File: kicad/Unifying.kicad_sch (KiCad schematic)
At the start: 38 parts

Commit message: Add files via upload
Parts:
- C1: renamed from U; value (none) -> 100n 50v; footprint (none) -> Capacitor_SMD:C_0402_1005Metric
- C10, C11, C2: renamed from U; value (none) -> 100n; footprint (none) -> Capacitor_SMD:C_0402_1005Metric
- C12: renamed from U; value (none) -> 1.2nF; footprint (none) -> Capacitor_SMD:C_0402_1005Metric
- C13, C14, C15, C16: renamed from U; value (none) -> 10u; footprint (none) -> Capacitor_SMD:C_0805_2012Metric
- C17: renamed from U; value (none) -> 100uF; footprint (none) -> Capacitor_Tantalum_SMD:CP_EIA-7343-31_Kemet-D
- C4, C5, C6, C7, C8, C9: renamed from U; value (none) -> 10u 10v; footprint (none) -> Capacitor_SMD:C_0805_2012Metric
- D1: renamed from U; value (none) -> MMBZ5242BLT3G; footprint (none) -> Diode_SMD:D_SOT-23_ANK
- H1, H2, H3, H4: renamed from U; value (none) -> MountingHole; footprint (none) -> MountingHole:MountingHole_2.7mm_M2.5
- H5, H6: renamed from U; value (none) -> M.2 Hole; footprint (none) -> MountingHole:M.2Hole_3.5mm
- J1: renamed from U; value (none) -> Conn_01x02; footprint (none) -> TerminalBlock:TerminalBlock_bornier-2_P5.08mm
- J2: renamed from U; value (none) -> Bus_M.2_Socket_B; footprint (none) -> CM4IO:Conn_TE-M.2-0.5-67P-doublesided
- L2: renamed from U; value (none) -> SRN6045TA-3R3Y (3.3uH); footprint (none) -> Inductor_SMD:L_Bourns_SRP7028A_7.3x6.6mm
- Q1: renamed from U; value (none) -> DMP3013SFV-7; footprint (none) -> Package_SON:Diodes_PowerDI3333-8
- R1, R4: renamed from U; value (none) -> 12K 1%; footprint (none) -> Resistor_SMD:R_0402_1005Metric
- R10: renamed from U; value (none) -> 15K 1%; footprint (none) -> Resistor_SMD:R_0402_1005Metric
- R11: renamed from U; value (none) -> 12K; footprint (none) -> Resistor_SMD:R_0402_1005Metric
- R3: renamed from U; value (none) -> 10R; footprint (none) -> Resistor_SMD:R_0402_1005Metric
- R5, R6, R7, R8: renamed from U; value (none) -> nf; footprint (none) -> Resistor_SMD:R_0402_1005Metric
- R9: renamed from U; value (none) -> 47K 1%; footprint (none) -> Resistor_SMD:R_0402_1005Metric
- U2: renamed from U; value (none) -> AP64501SP-13; footprint (none) -> Package_SO:SOIC-8-1EP_3.9x4.9mm_P1.27mm_EP2.95x4.9mm_Mask2.71x3.4mm_ThermalVias
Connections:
- net +3.3v: no longer J2.2 (3.3V), J2.4 (3.3V), J2.70 (3.3V), J2.72 (3.3V), J2.74 (3.3V), R11.2
- net +3.3vSSD: now also J2.2 (3.3V), J2.4 (3.3V), J2.70 (3.3V), J2.72 (3.3V), J2.74 (3.3V), R11.2; no longer R8.1
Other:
- note added: "+5V powers the CM4 module, high-speed connectors and USB connectors CM4 module has it's own 3.3V regulator"
- note added: "Connectors ------- Dual USB A USB OTG internal USB"
- note added: "PSU 5V -> 3.3v @ 3A for M.2"
- note removed: "Connectors ------- Dual USB A USB C OTG internal USB"
- note removed: "PSU 5V -> 3.3v @ 3A mainly for M.2"
- moved on the sheet: C1, C2, C4, C5, C6, C7, C8, C9, D1, J1, J2, Q1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

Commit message: Fixing remaining errors
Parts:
- U: renamed from H4; value MountingHole -> (none); footprint MountingHole:MountingHole_2.7mm_M2.5 -> (none)
- U: renamed from H3; value MountingHole -> (none); footprint MountingHole:MountingHole_2.7mm_M2.5 -> (none)
- U: renamed from H2; value MountingHole -> (none); footprint MountingHole:MountingHole_2.7mm_M2.5 -> (none)
- U: renamed from H1; value MountingHole -> (none); footprint MountingHole:MountingHole_2.7mm_M2.5 -> (none)
- U: renamed from C7; value 10u 10v -> (none); footprint Capacitor_SMD:C_0805_2012Metric -> (none)
- U: renamed from R11; value 12K -> (none); footprint Resistor_SMD:R_0402_1005Metric -> (none)
- U: renamed from C13; value 10u -> (none); footprint Capacitor_SMD:C_0805_2012Metric -> (none)
- U: renamed from R8; value nf -> (none); footprint Resistor_SMD:R_0402_1005Metric -> (none)
- U: renamed from C1; value 100n 50v -> (none); footprint Capacitor_SMD:C_0402_1005Metric -> (none)
- U: renamed from C6; value 10u 10v -> (none); footprint Capacitor_SMD:C_0805_2012Metric -> (none)
- U: renamed from R7; value nf -> (none); footprint Resistor_SMD:R_0402_1005Metric -> (none)
- U: renamed from C10; value 100n -> (none); footprint Capacitor_SMD:C_0402_1005Metric -> (none)
- U: renamed from D1; value MMBZ5242BLT3G -> (none); footprint Diode_SMD:D_SOT-23_ANK -> (none)
- U: renamed from C8; value 10u 10v -> (none); footprint Capacitor_SMD:C_0805_2012Metric -> (none)
- U: renamed from C12; value 1.2nF -> (none); footprint Capacitor_SMD:C_0402_1005Metric -> (none)
- U: renamed from R10; value 15K 1% -> (none); footprint Resistor_SMD:R_0402_1005Metric -> (none)
- U: renamed from C11; value 100n -> (none); footprint Capacitor_SMD:C_0402_1005Metric -> (none)
- U: renamed from Q1; value DMP3013SFV-7 -> (none); footprint Package_SON:Diodes_PowerDI3333-8 -> (none)
- U: renamed from R5; value nf -> (none); footprint Resistor_SMD:R_0402_1005Metric -> (none)
- U: renamed from R6; value nf -> (none); footprint Resistor_SMD:R_0402_1005Metric -> (none)
- U: renamed from L2; value SRN6045TA-3R3Y (3.3uH) -> (none); footprint Inductor_SMD:L_Bourns_SRP7028A_7.3x6.6mm -> (none)
- U: renamed from H6; value M.2 Hole -> (none); footprint MountingHole:M.2Hole_3.5mm -> (none)
- U: renamed from C17; value 100uF -> (none); footprint Capacitor_Tantalum_SMD:CP_EIA-7343-31_Kemet-D -> (none)
- U: renamed from C4; value 10u 10v -> (none); footprint Capacitor_SMD:C_0805_2012Metric -> (none)
- U: renamed from C15; value 10u -> (none); footprint Capacitor_SMD:C_0805_2012Metric -> (none)
- U: renamed from J2; value Bus_M.2_Socket_B -> (none); footprint CM4IO:Conn_TE-M.2-0.5-67P-doublesided -> (none)
- U: renamed from U2; value AP64501SP-13 -> (none); footprint Package_SO:SOIC-8-1EP_3.9x4.9mm_P1.27mm_EP2.95x4.9mm_Mask2.71x3.4mm_ThermalVias -> (none)
- U: renamed from C16; value 10u -> (none); footprint Capacitor_SMD:C_0805_2012Metric -> (none)
- U: renamed from C9; value 10u 10v -> (none); footprint Capacitor_SMD:C_0805_2012Metric -> (none)
- U: renamed from C5; value 10u 10v -> (none); footprint Capacitor_SMD:C_0805_2012Metric -> (none)
- U: renamed from R9; value 47K 1% -> (none); footprint Resistor_SMD:R_0402_1005Metric -> (none)
- U: renamed from R3; value 10R -> (none); footprint Resistor_SMD:R_0402_1005Metric -> (none)
- U: renamed from R4; value 12K 1% -> (none); footprint Resistor_SMD:R_0402_1005Metric -> (none)
- U: renamed from J1; value Conn_01x02 -> (none); footprint TerminalBlock:TerminalBlock_bornier-2_P5.08mm -> (none)
- U: renamed from C14; value 10u -> (none); footprint Capacitor_SMD:C_0805_2012Metric -> (none)
- U: renamed from C2; value 100n -> (none); footprint Capacitor_SMD:C_0402_1005Metric -> (none)
- U: renamed from H5; value M.2 Hole -> (none); footprint MountingHole:M.2Hole_3.5mm -> (none)
- U: renamed from R1; value 12K 1% -> (none); footprint Resistor_SMD:R_0402_1005Metric -> (none)
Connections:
- net +3.3vSSD: now also U.1

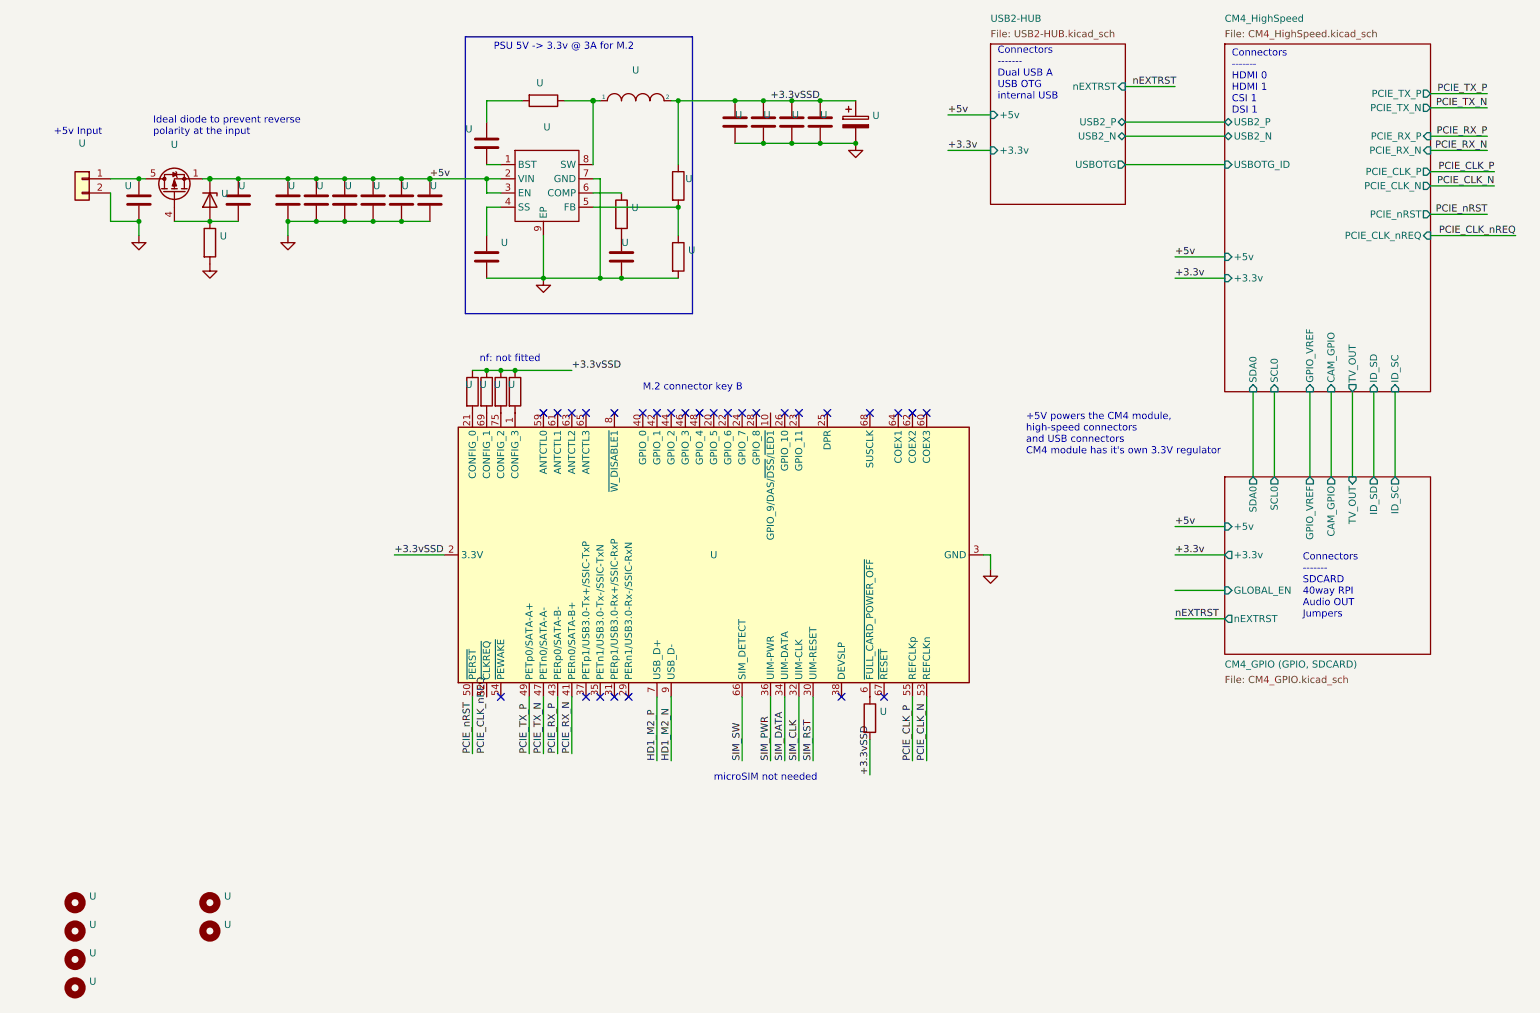
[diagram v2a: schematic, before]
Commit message: Mirroring CAM, DSI, new GPDI pinout fix #2 #3 #5 #12
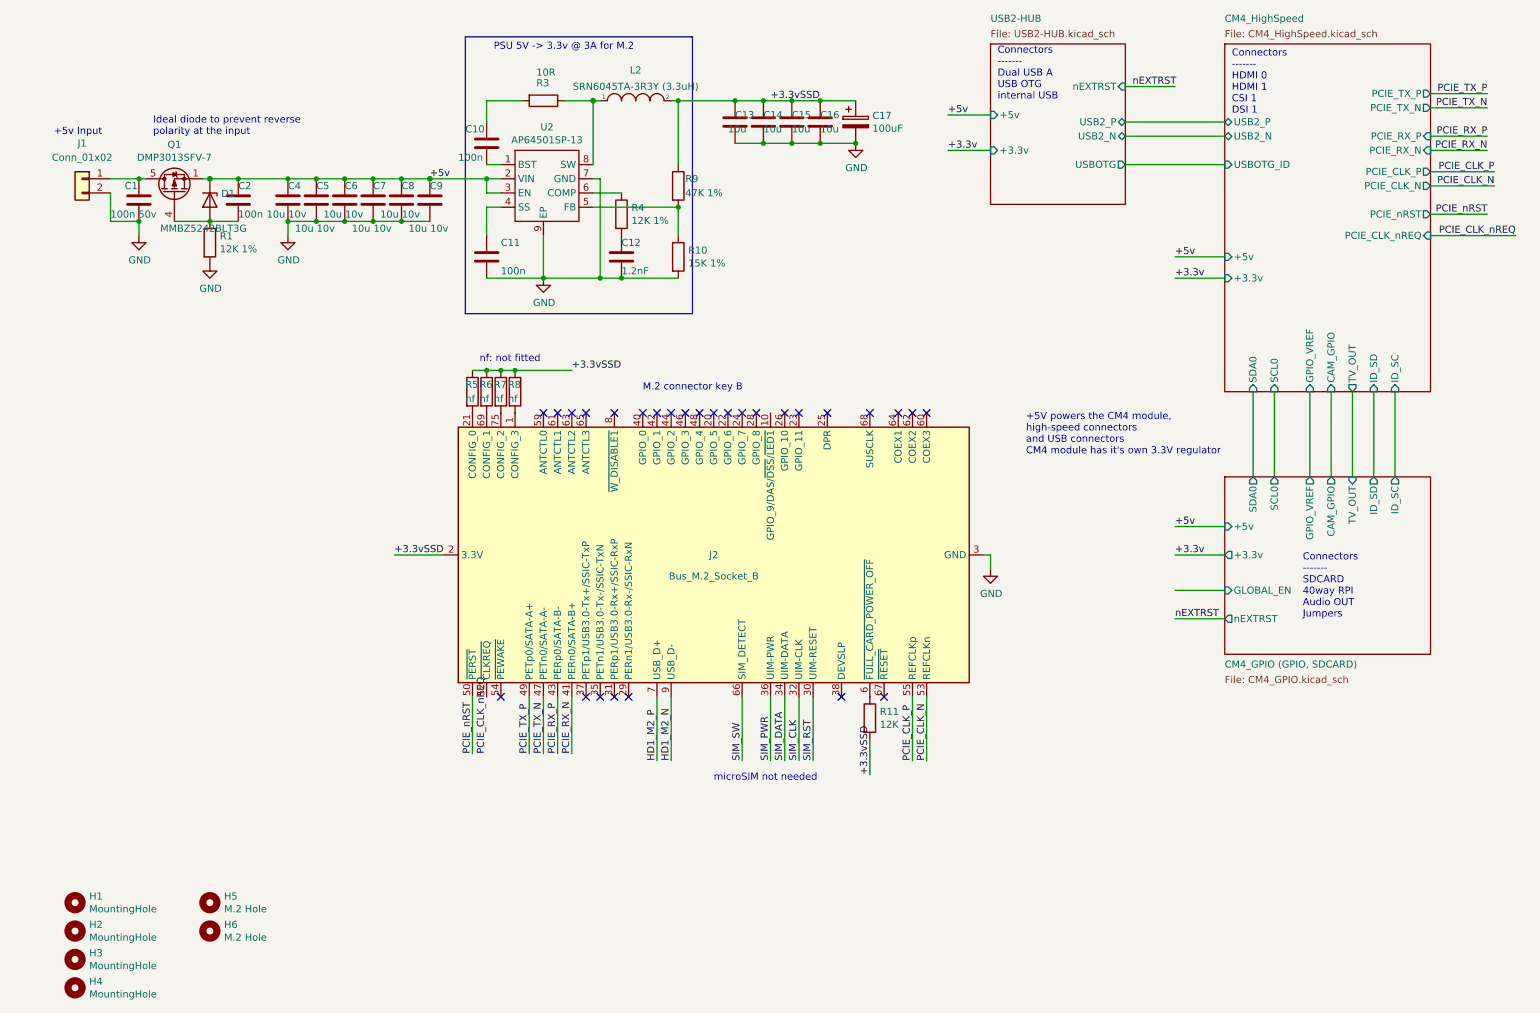
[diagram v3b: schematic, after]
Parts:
- C1: renamed from U; value (none) -> 100n 50v; footprint (none) -> Capacitor_SMD:C_0402_1005Metric
- C10, C11, C2: renamed from U; value (none) -> 100n; footprint (none) -> Capacitor_SMD:C_0402_1005Metric
- C12: renamed from U; value (none) -> 1.2nF; footprint (none) -> Capacitor_SMD:C_0402_1005Metric
- C13, C14, C15, C16: renamed from U; value (none) -> 10u; footprint (none) -> Capacitor_SMD:C_0805_2012Metric
- C17: renamed from U; value (none) -> 100uF; footprint (none) -> Capacitor_Tantalum_SMD:CP_EIA-7343-31_Kemet-D
- C4, C5, C6, C7, C8, C9: renamed from U; value (none) -> 10u 10v; footprint (none) -> Capacitor_SMD:C_0805_2012Metric
- D1: renamed from U; value (none) -> MMBZ5242BLT3G; footprint (none) -> Diode_SMD:D_SOT-23_ANK
- H1, H2, H3, H4: renamed from U; value (none) -> MountingHole; footprint (none) -> MountingHole:MountingHole_2.7mm_M2.5
- H5, H6: renamed from U; value (none) -> M.2 Hole; footprint (none) -> MountingHole:M.2Hole_3.5mm
- J1: renamed from U; value (none) -> Conn_01x02; footprint (none) -> TerminalBlock:TerminalBlock_bornier-2_P5.08mm
- J2: renamed from U; value (none) -> Bus_M.2_Socket_B; footprint (none) -> CM4IO:Conn_TE-M.2-0.5-67P-doublesided
- L2: renamed from U; value (none) -> SRN6045TA-3R3Y (3.3uH); footprint (none) -> Inductor_SMD:L_Bourns_SRP7028A_7.3x6.6mm
- Q1: renamed from U; value (none) -> DMP3013SFV-7; footprint (none) -> Package_SON:Diodes_PowerDI3333-8
- R1, R4: renamed from U; value (none) -> 12K 1%; footprint (none) -> Resistor_SMD:R_0402_1005Metric
- R10: renamed from U; value (none) -> 15K 1%; footprint (none) -> Resistor_SMD:R_0402_1005Metric
- R11: renamed from U; value (none) -> 12K; footprint (none) -> Resistor_SMD:R_0402_1005Metric
- R3: renamed from U; value (none) -> 10R; footprint (none) -> Resistor_SMD:R_0402_1005Metric
- R5, R6, R7, R8: renamed from U; value (none) -> nf; footprint (none) -> Resistor_SMD:R_0402_1005Metric
- R9: renamed from U; value (none) -> 47K 1%; footprint (none) -> Resistor_SMD:R_0402_1005Metric
- U2: renamed from U; value (none) -> AP64501SP-13; footprint (none) -> Package_SO:SOIC-8-1EP_3.9x4.9mm_P1.27mm_EP2.95x4.9mm_Mask2.71x3.4mm_ThermalVias
